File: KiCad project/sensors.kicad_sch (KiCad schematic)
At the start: 16 parts, among them J5 B4B-XH-AM__LF__SN_, Q1 TEMT6000X01, U6 BME280, U7 MAX4466EXK

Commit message: Fixed lots of bugs.
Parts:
- removed C16: 10u, Capacitor_SMD:C_0805_2012Metric, symbol SparkFun-Capacitor:C
- removed C18, C19: 0.1u, Capacitor_SMD:C_0805_2012Metric, symbol SparkFun-Capacitor:C
- removed C20: 1u, Capacitor_SMD:C_0805_2012Metric, symbol SparkFun-Capacitor:C
- removed R33, R35: 2K2, Resistor_SMD:R_0201_0603Metric, symbol Device:R
- removed R34: 100K, Resistor_SMD:R_0201_0603Metric, symbol Device:R
- removed U6: BME280, BME280:PSON65P250X250X100-8N, symbol BME280:BME280
- added C16, C18, C20: 100n, Capacitor_SMD:C_0805_2012Metric, symbol Device:C
- added C17: 10n, Capacitor_SMD:C_0805_2012Metric, symbol Device:C
- added C19: 1u, Capacitor_SMD:C_0805_2012Metric, symbol Device:C
- added R26, R28: 2K, Resistor_SMD:R_0805_2012Metric, symbol Device:R
- added R27, R29: 1M, Resistor_SMD:R_0805_2012Metric, symbol Device:R
- added R30: 10K, Resistor_SMD:R_0805_2012Metric, symbol Device:R
- added R31: 100K, Resistor_SMD:R_0805_2012Metric, symbol Device:R
- added U7: BME280, Project_Library:PSON65P250X250X100-8N, symbol BME280:BME280
- J4: renamed from J5; footprint B4B-XH-AM__LF__SN_:JST_B4B-XH-AM__LF__SN_ -> Project_Library:JST_B4B-XH-AM__LF__SN_
- MK1: footprint CMC-5042PF-AC:CUI_CMC-5042PF-AC -> Project_Library:CUI_CMC-5042PF-AC
- Q1: footprint TEMT6000X01:TRANS_TEMT6000X01 -> Project_Library:TRANS_TEMT6000X01
- R23: renamed from R32; footprint Resistor_SMD:R_0201_0603Metric -> Resistor_SMD:R_0805_2012Metric
- R24: renamed from R30; footprint Resistor_SMD:R_0201_0603Metric -> Resistor_SMD:R_0805_2012Metric
- R25: renamed from R31; footprint Resistor_SMD:R_0201_0603Metric -> Resistor_SMD:R_0805_2012Metric
- U8: renamed from U7; footprint MAX4466EXK:SOT65P210X110-5N -> Project_Library:SOT65P210X110-5N
- renumbered C17 to C15
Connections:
- net 3.3V: now also U8.5 (VCC), C18.1, R26.2, R27.2, U7.2 (CSB), U7.6 (VDDIO), U7.8 (VDD)
- net GND: now also C16.2, C18.2, C19.1, R29.1, U7.1 (GND), U7.5 (SDO), U7.7 (GND)
- net MIC_OUT: now also C20.2, R31.2
- net SCL: now also U7.4 (SCK)
- net SDA: now also U7.3 (SDI)
- net at U8.3 (IN-): now also C20.1, R30.2, R31.1
- net at MK1.OUT: now also C17.2, R28.1
- net at U8.1 (IN+): now also C17.1, R27.1, R29.2
- new net: C19.2, R30.1
- new net: C16.1, R26.1, R28.2
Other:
- moved on the sheet: C15, MK1, U8

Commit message: Completed draft layout.
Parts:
- removed J4: B4B-XH-AM__LF__SN_, Project_Library:JST_B4B-XH-AM__LF__SN_, symbol B4B-XH-AM__LF__SN_:B4B-XH-AM__LF__SN_
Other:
- note removed: "OLED display connector (I2C)"

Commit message: Replaced the button, USB, bat connector with new symbols and footprints. Completed draft layout and routing.
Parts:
- C16, C18, C20: value 100n -> 0.1u
- MK1: Manufacturer_Part_Number (none) -> CMC-5042PF-AC
- Q1: Manufacturer_Part_Number (none) -> TEMT6000X01; PACKAGE (none) -> 4 mm x 2 mm x 1.05 mm
- R23, R24, R25, R26, R27, R28, R29, R30, R31: PACKAGE (none) -> 0805
- U7: MANUFACTURER (none) -> Bosch; Manufacturer_Part_Number (none) -> BME280; PACKAGE LGA-8 Bosch -> LGA-8
- U8: value MAX4466EXK -> MAX4466EXK+T; MANUFACTURER (none) -> Analog Devices Inc.; Manufacturer_Part_Number (none) -> MAX4466EXK+T; PACKAGE (none) -> SC-70-5
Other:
- moved on the sheet: C16, C17, C18, C19, C20, MK1, Q1, R23, R26, R27, R28, R29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

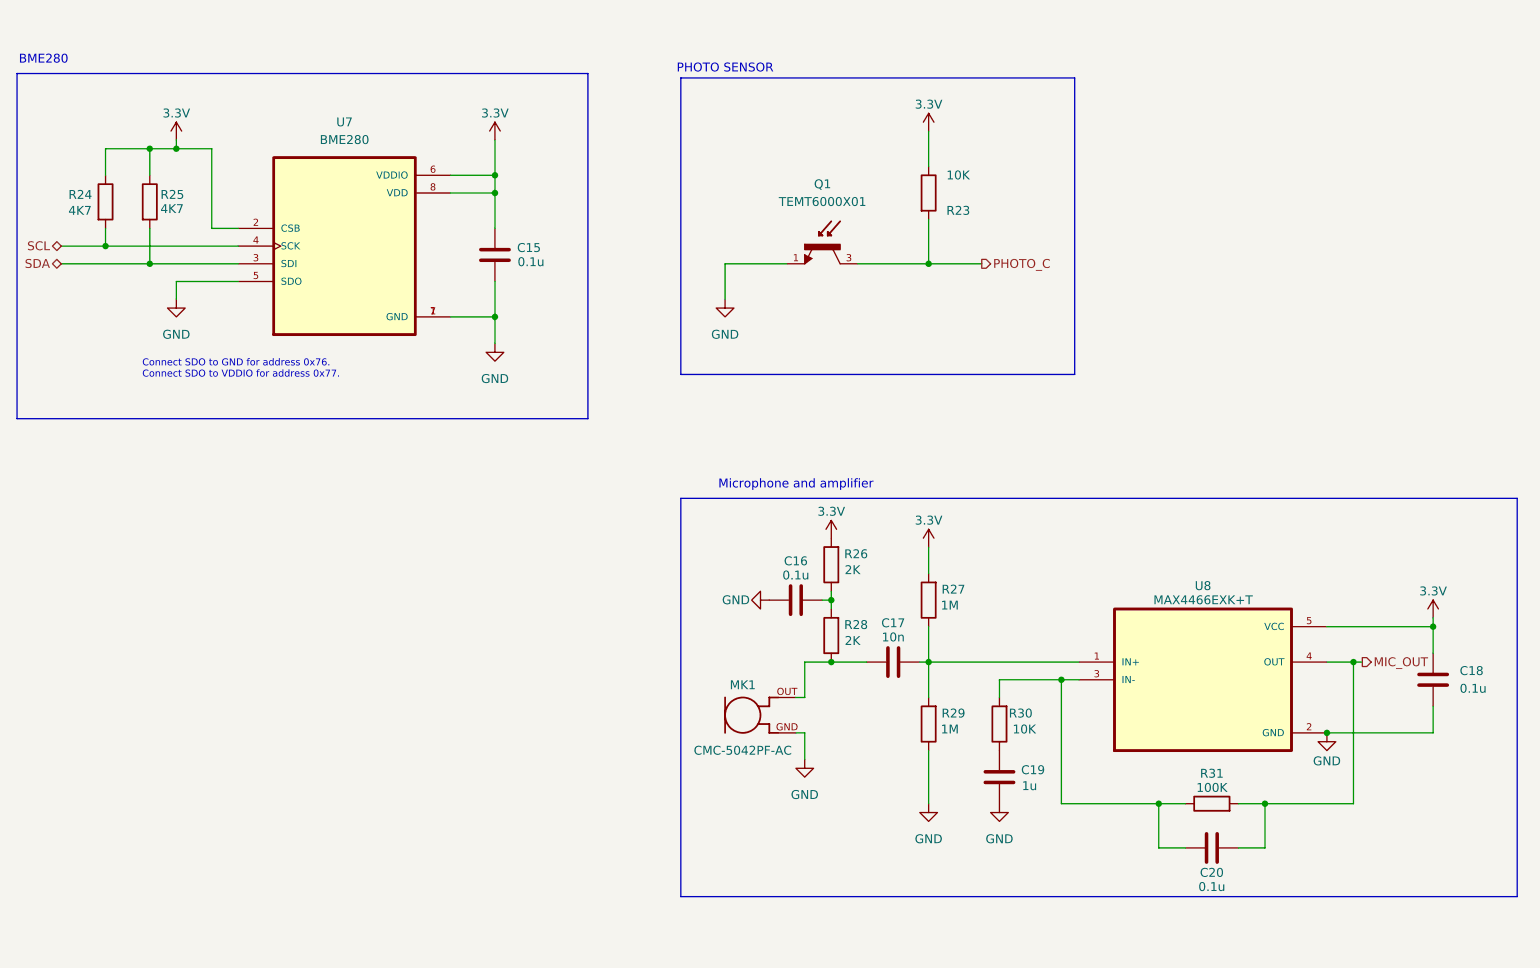
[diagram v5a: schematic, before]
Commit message: Fixed and improved Schematic design:
* Changed the buttons
* Added a ferrite bead at the output of the charger to cut some possible noise.
* Changed the values of R30, R31 and C19, and i add a 100K trimmer to set the gain from 25x to 125x.
* Added C23, C24 and C25 in the photo sensor circuit
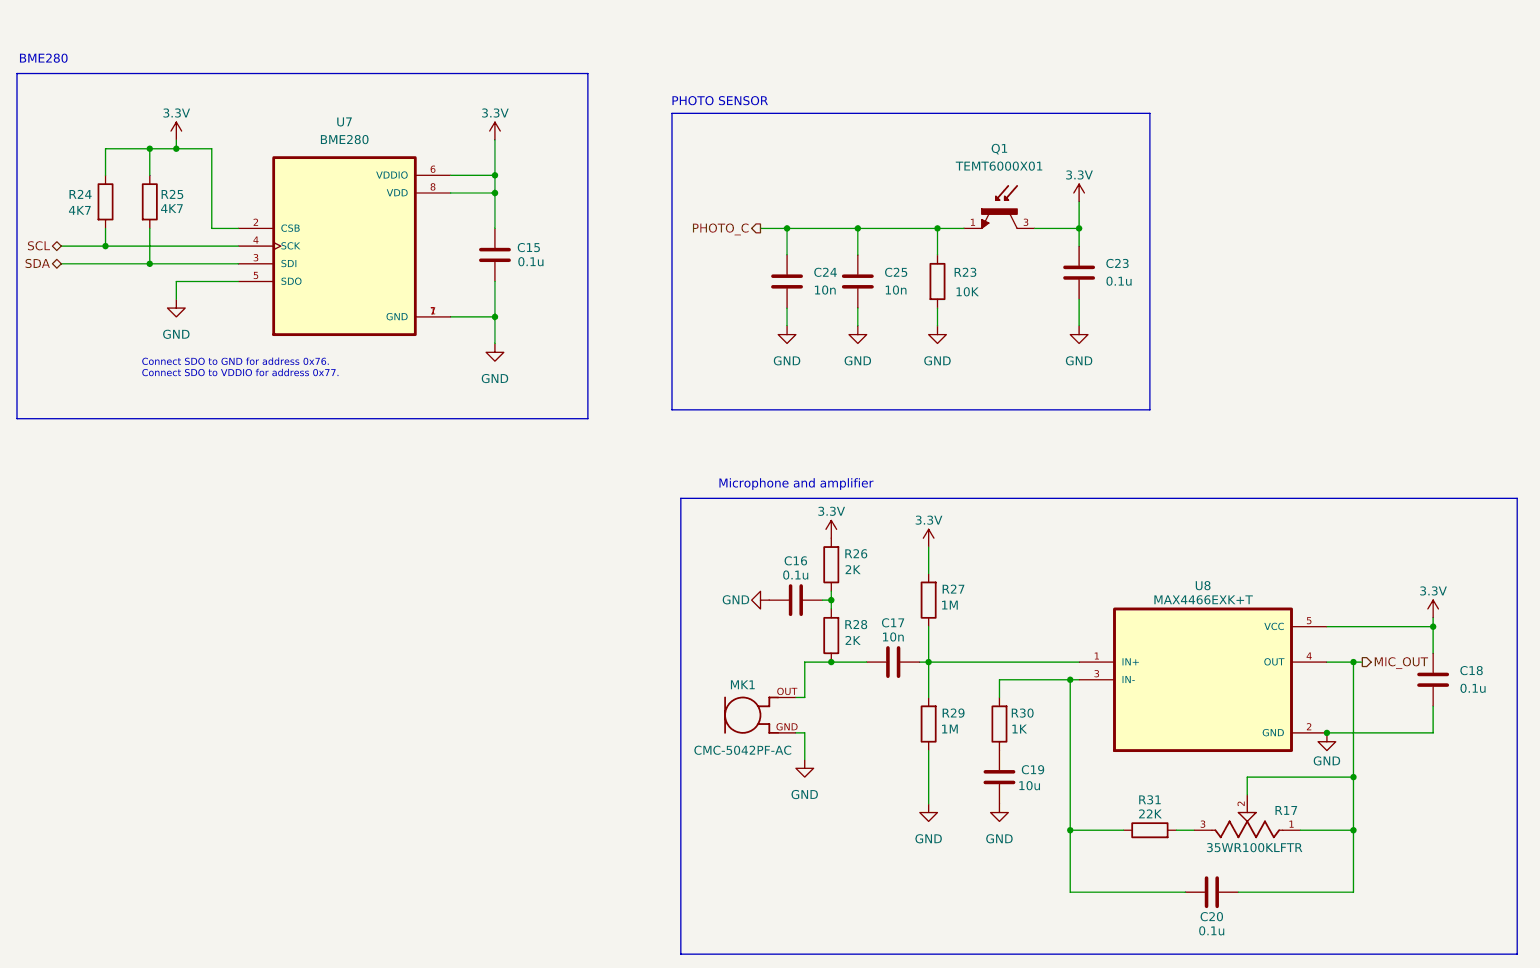
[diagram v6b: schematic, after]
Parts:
- added C23: 0.1u, symbol Device:C
- added C24, C25: 10n, symbol Device:C
- added R17: 35WR100KLFTR, 35WR100KLFTR:TRIM_35WR100KLFTR, symbol 35WR100KLFTR:35WR100KLFTR
- C19: value 1u -> 10u
- R30: value 10K -> 1K
- R31: value 100K -> 22K
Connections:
- net 3.3V: now also Q1.3, C23.1; no longer R23.1
- net GND: now also R23.2, C23.2, C24.2, C25.2; no longer Q1.1
- net MIC_OUT: now also R17.1, R17.2; no longer R31.2
- net PHOTO_C: now also Q1.1, R23.1, C24.1, C25.1; no longer Q1.3, R23.2
- new net: R17.3, R31.2
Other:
- moved on the sheet: C20, Q1, R23, R31

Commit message: Completed schematic fixes and updates. Continuing with the layout for Prototype #2.
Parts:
- C23, C24, C25: footprint (none) -> Capacitor_SMD:C_0805_2012Metric
- MK1: footprint Project_Library:CUI_CMC-5042PF-AC -> Footprints:CUI_CMC-5042PF-AC
- Q1: footprint Project_Library:TRANS_TEMT6000X01 -> Footprints:TRANS_TEMT6000X01
- R17: footprint 35WR100KLFTR:TRIM_35WR100KLFTR -> Footprints:TRIM_35WR100KLFTR
- U7: footprint Project_Library:PSON65P250X250X100-8N -> Footprints:PSON65P250X250X100-8N
- U8: footprint Project_Library:SOT65P210X110-5N -> Footprints:SOT65P210X110-5N
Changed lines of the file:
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@@
 			)
 		)
-		(property "Footprint" "Project_Library:CUI_CMC-5042PF-AC"
+		(property "Footprint" "Footprints:CUI_CMC-5042PF-AC"
 			(at 125.73 121.92 0)
 			(effects
@@
 			)
 		)
-		(property "Footprint" "Project_Library:PSON65P250X250X100-8N"
+		(property "Footprint" "Footprints:PSON65P250X250X100-8N"
 			(at 68.58 54.61 0)
 			(effects
@@
 			)
 		)
-		(property "Footprint" ""
+		(property "Footprint" "Capacitor_SMD:C_0805_2012Metric"
 			(at 143.2052 63.5 0)
 			(effects
@@
 			)
 		)
-		(property "Footprint" ""
+		(property "Footprint" "Capacitor_SMD:C_0805_2012Metric"
 			(at 174.9552 62.23 0)
 			(effects
@@
 			)
 		)
-		(property "Footprint" ""
+		(property "Footprint" "Capacitor_SMD:C_0805_2012Metric"
 			(at 133.0452 63.5 0)
 			(effects
@@
 			)
 		)
-		(property "Footprint" "Project_Library:SOT65P210X110-5N"
+		(property "Footprint" "Footprints:SOT65P210X110-5N"
 			(at 191.77 116.84 0)
 			(effects
@@
 			)
 		)
-		(property "Footprint" "35WR100KLFTR:TRIM_35WR100KLFTR"
+		(property "Footprint" "Footprints:TRIM_35WR100KLFTR"
 			(at 198.12 138.43 0)
 			(effects
@@
 			)
 		)
-		(property "Footprint" "Project_Library:TRANS_TEMT6000X01"
+		(property "Footprint" "Footprints:TRANS_TEMT6000X01"
 			(at 162.56 49.53 0)
 			(effects

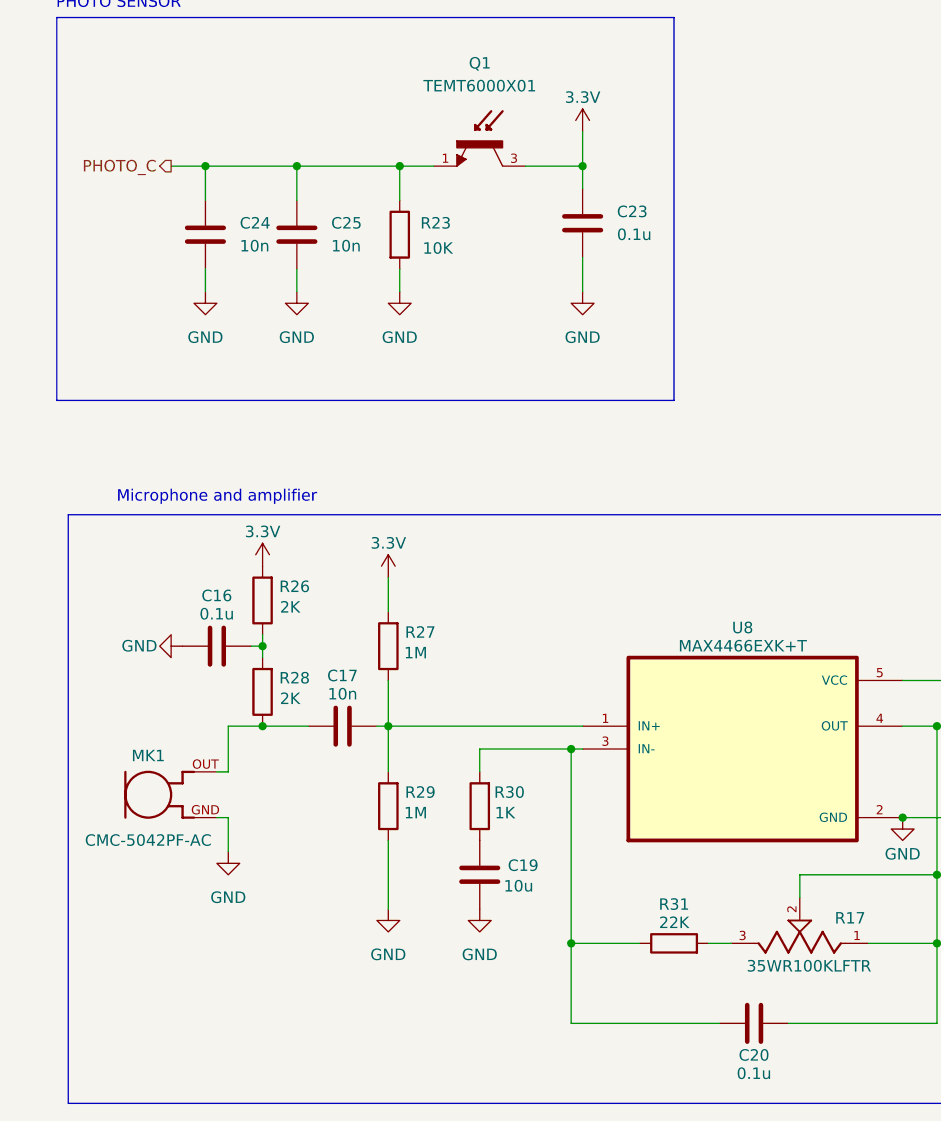
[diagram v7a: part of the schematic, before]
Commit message: Finished layout update for prototype #2.
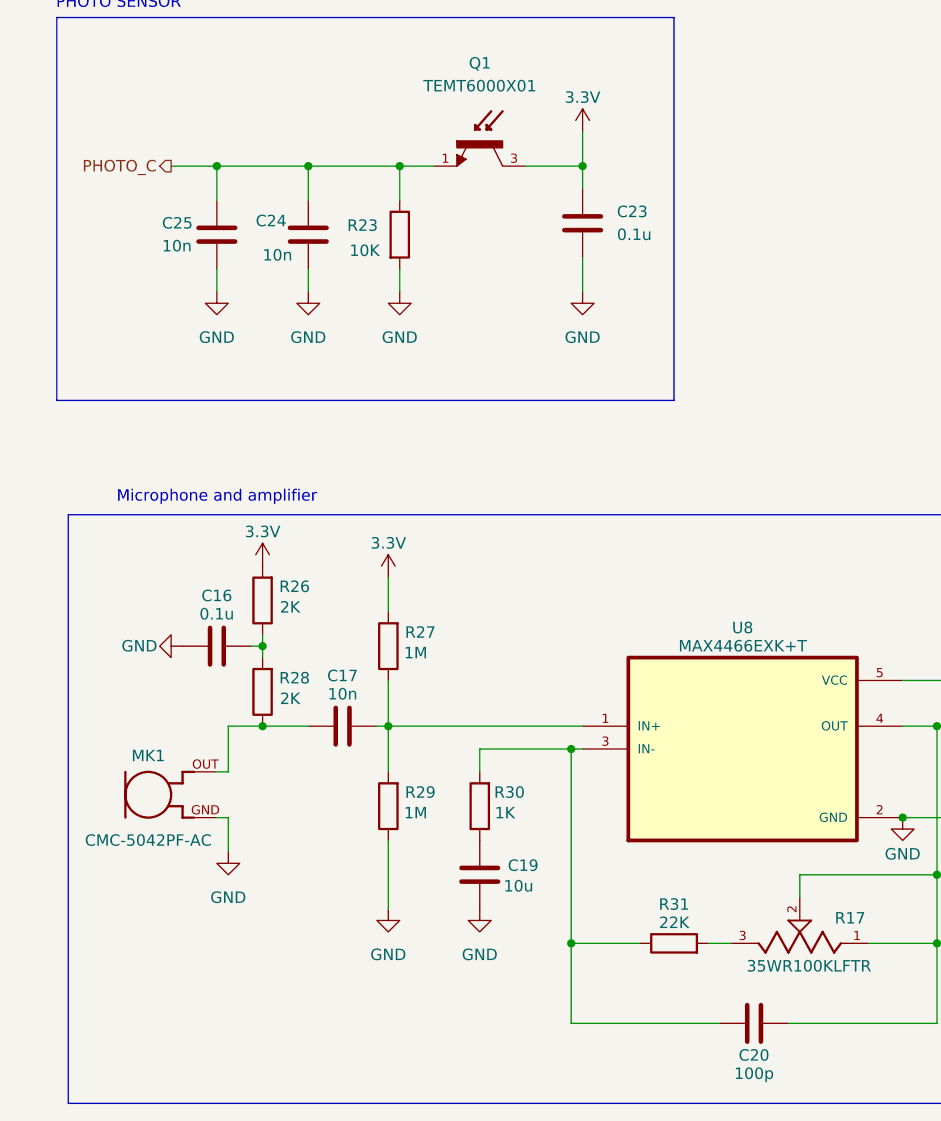
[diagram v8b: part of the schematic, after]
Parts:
- C20: value 0.1u -> 100p
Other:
- moved on the sheet: C24, C25
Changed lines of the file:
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@@
 	)
 	(junction
+		(at 133.35 52.07)
+		(diameter 0)
+		(color 0 0 0 0)
+	)
+	(junction
 		(at 213.36 138.43)
 		(diameter 0)
@@
 	)
 	(junction
-		(at 132.08 52.07)
+		(at 143.51 52.07)
 		(diameter 0)
 		(color 0 0 0 0)
@@
 	)
 	(junction
-		(at 142.24 52.07)
-		(diameter 0)
-		(color 0 0 0 0)
-	)
-	(junction
 		(at 209.55 124.46)
 		(diameter 0)
@@
 	(wire
 		(pts
-			(xy 128.27 52.07) (xy 132.08 52.07)
+			(xy 128.27 52.07) (xy 133.35 52.07)
 		)
 		(stroke
@@
 	(wire
 		(pts
-			(xy 132.08 52.07) (xy 142.24 52.07)
-		)
-		(stroke
-			(width 0)
-			(type default)
-		)
-	)
-	(wire
-		(pts
 			(xy 173.99 54.61) (xy 173.99 52.07)
 		)
@@
 	(wire
 		(pts
-			(xy 132.08 63.5) (xy 132.08 66.04)
+			(xy 143.51 63.5) (xy 143.51 66.04)
 		)
 		(stroke
@@
 	(wire
 		(pts
-			(xy 132.08 55.88) (xy 132.08 52.07)
+			(xy 143.51 55.88) (xy 143.51 52.07)
+		)
+		(stroke
+			(width 0)
+			(type default)
+		)
+	)
+	(wire
+		(pts
+			(xy 133.35 52.07) (xy 143.51 52.07)
 		)
 		(stroke
@@
 	(wire
 		(pts
-			(xy 142.24 52.07) (xy 142.24 55.88)
+			(xy 133.35 52.07) (xy 133.35 55.88)
 		)
 		(stroke
@@
 	(wire
 		(pts
-			(xy 142.24 63.5) (xy 142.24 66.04)
+			(xy 133.35 63.5) (xy 133.35 66.04)
 		)
 		(stroke
@@
 	(wire
 		(pts
-			(xy 142.24 52.07) (xy 153.67 52.07)
+			(xy 173.99 48.26) (xy 173.99 52.07)
 		)
 		(stroke
@@
 	(wire
 		(pts
-			(xy 173.99 48.26) (xy 173.99 52.07)
+			(xy 27.94 57.15) (xy 40.64 57.15)
 		)
 		(stroke
@@
 	(wire
 		(pts
-			(xy 27.94 57.15) (xy 40.64 57.15)
+			(xy 27.94 54.61) (xy 34.29 54.61)
 		)
 		(stroke
@@
 	(wire
 		(pts
-			(xy 27.94 54.61) (xy 34.29 54.61)
+			(xy 83.82 46.99) (xy 90.17 46.99)
 		)
 		(stroke
@@
 	(wire
 		(pts
-			(xy 83.82 46.99) (xy 90.17 46.99)
+			(xy 143.51 52.07) (xy 153.67 52.07)
 		)
 		(stroke
@@
 	(symbol
 		(lib_id "power:GND")
-		(at 132.08 66.04 0)
+		(at 143.51 66.04 0)
 		(unit 1)
 		(exclude_from_sim no)
@@
 		(fields_autoplaced yes)
 		(property "Reference" "#PWR064"
-			(at 132.08 72.39 0)
+			(at 143.51 72.39 0)
 			(effects
 				(font
@@
 		)
 		(property "Value" "GND"
-			(at 132.08 71.12 0)
+			(at 143.51 71.12 0)
 			(effects
 				(font
@@
 		)
 		(property "Footprint" ""
-			(at 132.08 66.04 0)
+			(at 143.51 66.04 0)
 			(effects
 				(font
@@
 		)
 		(property "Datasheet" ""
-			(at 132.08 66.04 0)
+			(at 143.51 66.04 0)
 			(effects
 				(font
@@
 		)
 		(property "Description" "Power symbol creates a global label with name \"GND\" , ground"
-			(at 132.08 66.04 0)
+			(at 143.51 66.04 0)
 			(effects
 				(font
@@
 	(symbol
 		(lib_id "power:GND")
-		(at 142.24 66.04 0)
+		(at 133.35 66.04 0)
 		(unit 1)
 		(exclude_from_sim no)
@@
 		(fields_autoplaced yes)
 		(property "Reference" "#PWR063"
-			(at 142.24 72.39 0)
+			(at 133.35 72.39 0)
 			(effects
 				(font
@@
 		)
 		(property "Value" "GND"
-			(at 142.24 71.12 0)
+			(at 133.35 71.12 0)
 			(effects
 				(font
@@
 		)
 		(property "Footprint" ""
-			(at 142.24 66.04 0)
+			(at 133.35 66.04 0)
 			(effects
 				(font
@@
 		)
 		(property "Datasheet" ""
-			(at 142.24 66.04 0)
+			(at 133.35 66.04 0)
 			(effects
 				(font
@@
 		)
 		(property "Description" "Power symbol creates a global label with name \"GND\" , ground"
-			(at 142.24 66.04 0)
+			(at 133.35 66.04 0)
 			(effects
 				(font
@@
 	(symbol
 		(lib_id "Device:C")
-		(at 142.24 59.69 0)
+		(at 133.35 59.69 0)
 		(unit 1)
 		(exclude_from_sim no)
@@
 		(on_board yes)
 		(dnp no)
-		(fields_autoplaced yes)
 		(property "Reference" "C25"
-			(at 146.05 58.4199 0)
+			(at 127.254 58.42 0)
 			(effects
 				(font
@@
 		)
 		(property "Value" "10n"
-			(at 146.05 60.9599 0)
+			(at 127.254 60.96 0)
 			(effects
 				(font
@@
 		)
 		(property "Footprint" "Capacitor_SMD:C_0805_2012Metric"
-			(at 143.2052 63.5 0)
+			(at 134.3152 63.5 0)
 			(effects
 				(font
@@
 		)
 		(property "Datasheet" "~"
-			(at 142.24 59.69 0)
+			(at 133.35 59.69 0)
 			(effects
 				(font
@@
 		)
 		(property "Description" "Unpolarized capacitor"
-			(at 142.24 59.69 0)
+			(at 133.35 59.69 0)
 			(effects
 				(font
@@
 		)
 		(property "Comments" ""
-			(at 142.24 59.69 0)
+			(at 133.35 59.69 0)
 			(effects
 				(font
@@
 	(symbol
 		(lib_id "Device:C")
-		(at 132.08 59.69 0)
+		(at 143.51 59.69 0)
 		(unit 1)
 		(exclude_from_sim no)
@@
 		(on_board yes)
 		(dnp no)
-		(fields_autoplaced yes)
 		(property "Reference" "C24"
-			(at 135.89 58.4199 0)
+			(at 137.668 58.166 0)
 			(effects
 				(font
@@
 		)
 		(property "Value" "10n"
-			(at 135.89 60.9599 0)
+			(at 138.43 61.976 0)
 			(effects
 				(font
@@
 		)
 		(property "Footprint" "Capacitor_SMD:C_0805_2012Metric"
-			(at 133.0452 63.5 0)
+			(at 144.4752 63.5 0)
 			(effects
 				(font
@@
 		)
 		(property "Datasheet" "~"
-			(at 132.08 59.69 0)
+			(at 143.51 59.69 0)
 			(effects
 				(font
@@
 		)
 		(property "Description" "Unpolarized capacitor"
-			(at 132.08 59.69 0)
+			(at 143.51 59.69 0)
 			(effects
 				(font
@@
 		)
 		(property "Comments" ""
-			(at 132.08 59.69 0)
+			(at 143.51 59.69 0)
 			(effects
 				(font
@@
 			)
 		)
-		(property "Value" "0.1u"
+		(property "Value" "100p"
 			(at 193.04 152.908 90)
 			(effects
@@
 		(dnp no)
 		(property "Reference" "R23"
-			(at 155.956 58.42 0)
+			(at 147.828 58.674 0)
 			(effects
 				(font
@@
 		)
 		(property "Value" "10K"
-			(at 156.21 61.214 0)
+			(at 148.082 61.468 0)
 			(effects
 				(font
